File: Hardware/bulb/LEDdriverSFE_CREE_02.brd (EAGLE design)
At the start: 49 x 49 mm, 26 parts, among them U1 ZXLD1360, U2 ZXLD1360, U3 ZXLD1360, U4 ZXLD1360

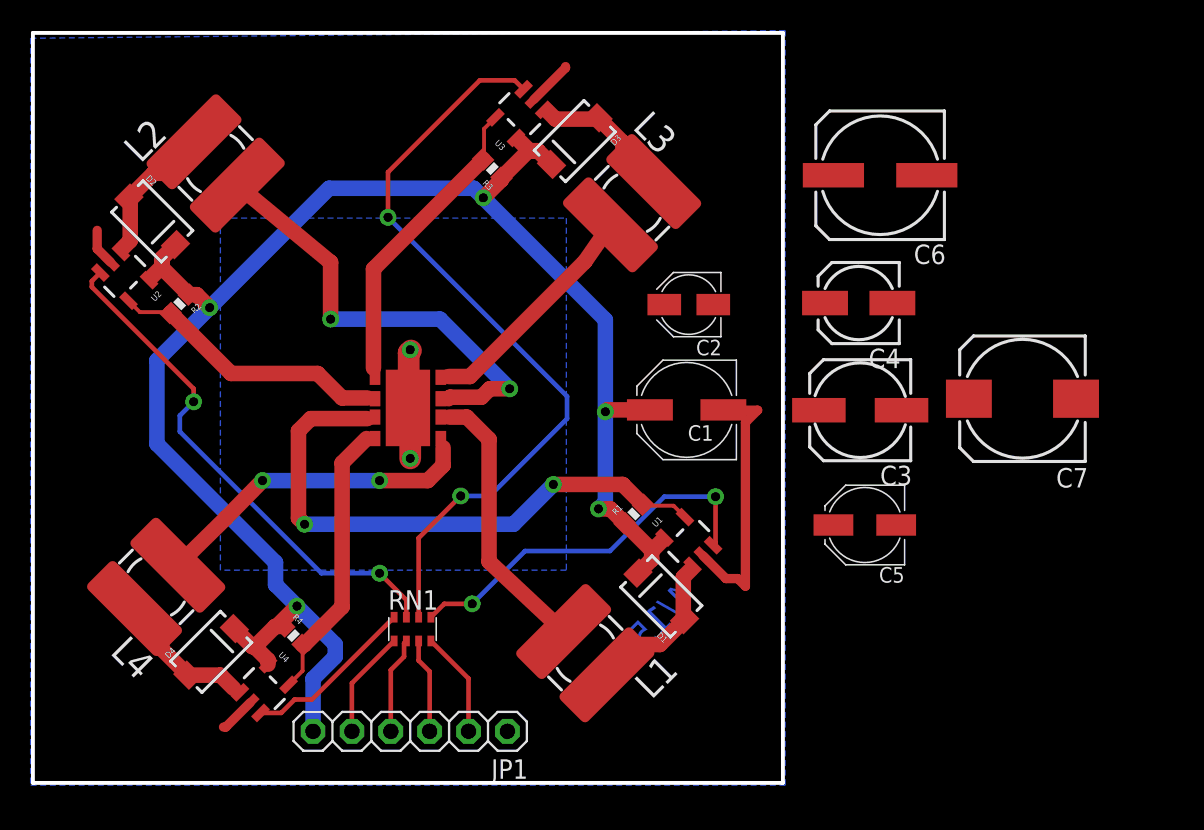
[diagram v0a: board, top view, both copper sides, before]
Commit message: added firmware version 08 and included updates to server
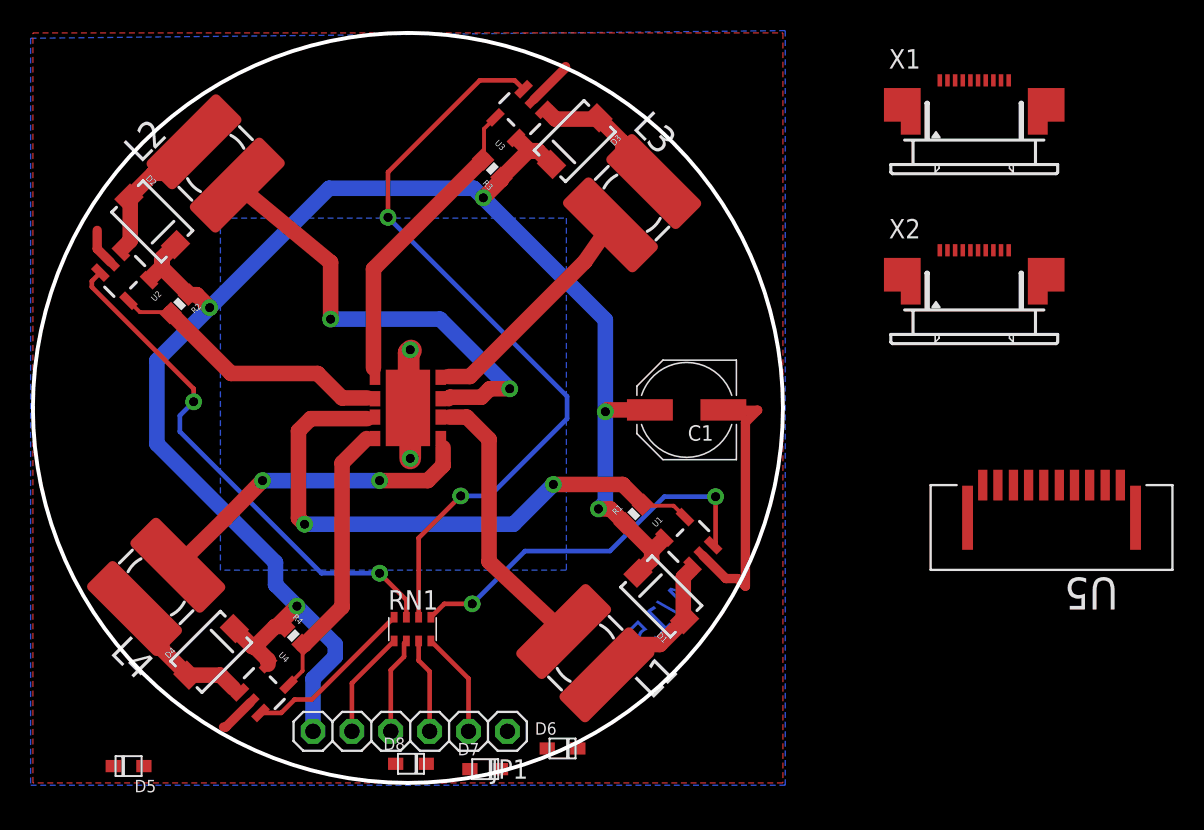
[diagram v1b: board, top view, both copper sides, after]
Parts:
- removed C2: (no value), rcl:PANASONIC_B
- removed C3: (no value), rcl:153CLV-0605
- removed C4: (no value), rcl:153CLV-0505
- removed C5: (no value), rcl:PANASONIC_C
- removed C6: (no value), rcl:153CLV-0807
- removed C7: (no value), rcl:175TMP-0808
- added D5, D6, D7, D8: (no value), adafruit:SOD-323F
- added U5: SFW10R-1STE1LF, FCI_By_element14_Batch_1:FCI_SFW10R-1STE1LF
- added X1, X2: 52745-1090, con-molex:52745-1090
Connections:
- removed net N$15: JP1.5, RN1.1
- removed net N$18: JP1.3, RN1.3
- new net BLUEIN: D7.C, JP1.4, RN1.2
- new net D+IN: X1.7, X2.7
- new net D-IN: X1.8, X2.8
- new net D10: X1.4, X2.4
- new net D13: X1.2, X2.2
- new net D5: X1.3, X2.3
- new net D9: X1.5, X2.5
- new net GREENIN: D6.C, JP1.2, RN1.4
- new net N$20: D7.A
- new net N$21: D8.A
- new net RAW: X1.10, X2.10
- new net REDIN: D5.C, JP1.5, RN1.1
- new net TXLED: X1.6, X2.6
- new net UVCC: X1.1, X2.1
- new net WHITEIN: D8.C, JP1.3, RN1.3
- net GND: now also X1.9, X2.9
- net N$14: now also D5.A; no longer JP1.2, RN1.4
- net N$17: now also D6.A; no longer JP1.4, RN1.2
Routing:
- net REDIN: track 0.00 -> 7.05 mm
- net N$15: track 7.05 -> 0.00 mm
- net N$14: track 6.92 -> 0.00 mm
- net GREENIN: track 0.00 -> 6.92 mm
- net N$17: track 6.33 -> 0.00 mm
- net BLUEIN: track 0.00 -> 6.33 mm
- net WHITEIN: track 0.00 -> 6.20 mm
- net N$18: track 6.20 -> 0.00 mm
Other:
- outline, holes or cut-outs redrawn
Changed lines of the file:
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@@
 <?xml version="1.0" encoding="utf-8"?>
 <!DOCTYPE eagle SYSTEM "eagle.dtd">
-<eagle version="6.2">
+<eagle version="6.4">
 <drawing>
 <settings>
@@
 <layer number="19" name="Unrouted" color="12" fill="1" visible="yes" active="yes"/>
 <layer number="20" name="Dimension" color="15" fill="1" visible="yes" active="yes"/>
-<layer number="21" name="tPlace" color="16" fill="1" visible="yes" active="yes"/>
+<layer number="21" name="tPlace" color="16" fill="1" visible="no" active="yes"/>
 <layer number="22" name="bPlace" color="14" fill="1" visible="no" active="yes"/>
 <layer number="23" name="tOrigins" color="15" fill="1" visible="yes" active="yes"/>
@@
 <text x="-4.191" y="19.431" size="1.778" layer="22" ratio="15" rot="SMR270">GND</text>
 <text x="8.001" y="21.971" size="1.27" layer="22" ratio="15" rot="SMR270">12-30V</text>
-<wire x1="0" y1="49" x2="49" y2="49" width="0.254" layer="20"/>
-<wire x1="49" y1="49" x2="49" y2="0" width="0.254" layer="20"/>
-<wire x1="49" y1="0" x2="0" y2="0" width="0.254" layer="20"/>
-<wire x1="0" y1="0" x2="0" y2="49" width="0.254" layer="20"/>
 <rectangle x1="3" y1="30.85" x2="8.4" y2="35.55" layer="41"/>
 <rectangle x1="12.85" y1="4" x2="17.4" y2="8.45" layer="41"/>
@@
 <rectangle x1="28.9" y1="41.4" x2="34.5" y2="46.4" layer="41"/>
 <rectangle x1="20.75" y1="21.4" x2="27.75" y2="28.2" layer="41"/>
+<wire x1="0" y1="24.5" x2="24.5" y2="49" width="0.254" layer="20" curve="-90"/>
+<wire x1="0" y1="24.5" x2="24.5" y2="0" width="0.254" layer="20" curve="90"/>
+<wire x1="49" y1="24.5" x2="24.5" y2="0" width="0.254" layer="20" curve="-90"/>
+<wire x1="49" y1="24.5" x2="24.5" y2="49" width="0.254" layer="20" curve="90"/>
 </plain>
 <attributes>
@@
 <class number="0" name="default" width="0" drill="0">
 </class>
+<class number="1" name="vcc" width="0" drill="0">
+</class>
 </classes>
-<designrules>
+<designrules name="default">
 <description language="en">&lt;b&gt;EAGLE Design Rules&lt;/b&gt;
 &lt;p&gt;
@@
 <attribute name="OC_FARNELL" value="unknown" x="24.8" y="10.05" size="1.778" layer="27" display="off"/>
 </element>
-<element name="C2" library="rcl" package="PANASONIC_B" value="" x="42.85" y="31.25" rot="R180"/>
-<element name="C3" library="rcl" package="153CLV-0605" value="" x="54.05" y="24.35" rot="R180"/>
-<element name="C4" library="rcl" package="153CLV-0505" value="" x="53.95" y="31.35" rot="R180"/>
-<element name="C5" library="rcl" package="PANASONIC_C" value="" x="54.35" y="16.85" rot="R180"/>
-<element name="C6" library="rcl" package="153CLV-0807" value="" x="55.35" y="39.7" rot="R180"/>
-<element name="C7" library="rcl" package="175TMP-0808" value="" x="64.65" y="25.1" rot="R180"/>
+<element name="D5" library="adafruit" package="SOD-323F" value="" x="6.25" y="1.1" rot="R180"/>
+<element name="D6" library="adafruit" package="SOD-323F" value="" x="34.6" y="2.25"/>
+<element name="D7" library="adafruit" package="SOD-323F" value="" x="29.55" y="0.9"/>
+<element name="D8" library="adafruit" package="SOD-323F" value="" x="24.7" y="1.25"/>
+<element name="X1" library="con-molex" package="52745-1090" value="52745-1090" x="61.5" y="43.4">
+<attribute name="OC_NEWARK" value="92M6380" x="61.5" y="43.4" size="1.778" layer="27" display="off"/>
+<attribute name="MPN" value="52745-1090" x="61.5" y="43.4" size="1.778" layer="27" display="off"/>
+<attribute name="MF" value="" x="61.5" y="43.4" size="1.778" layer="27" display="off"/>
+<attribute name="OC_FARNELL" value="unknown" x="61.5" y="43.4" size="1.778" layer="27" display="off"/>
+</element>
+<element name="X2" library="con-molex" package="52745-1090" value="52745-1090" x="61.5" y="32.3">
+<attribute name="OC_NEWARK" value="92M6380" x="61.5" y="32.3" size="1.778" layer="27" display="off"/>
+<attribute name="MPN" value="52745-1090" x="61.5" y="32.3" size="1.778" layer="27" display="off"/>
+<attribute name="MF" value="" x="61.5" y="32.3" size="1.778" layer="27" display="off"/>
+<attribute name="OC_FARNELL" value="unknown" x="61.5" y="32.3" size="1.778" layer="27" display="off"/>
+</element>
+<element name="U5" library="FCI_By_element14_Batch_1" package="FCI_SFW10R-1STE1LF" value="SFW10R-1STE1LF" x="66.55" y="22.2" rot="R180">
+<attribute name="PACKAGE" value="CONNECTOR - 10POS" x="66.55" y="22.2" size="1.778" layer="27" rot="R180" display="off"/>
+<attribute name="OC_NEWARK" value="62K5594" x="66.55" y="22.2" size="1.778" layer="27" rot="R180" display="off"/>
+<attribute name="MPN" value="SFW10R-1STE1LF" x="66.55" y="22.2" size="1.778" layer="27" rot="R180" display="off"/>
+<attribute name="SUPPLIER" value="FCI" x="66.55" y="22.2" size="1.778" layer="27" rot="R180" display="off"/>
+<attribute name="OC_FARNELL" value="1632207" x="66.55" y="22.2" size="1.778" layer="27" rot="R180" display="off"/>
+</element>
 </elements>
 <signals>
@@
 <wire x1="46.55" y1="12.85" x2="46.05" y2="13.35" width="0.6096" layer="1"/>
 <wire x1="46.05" y1="13.35" x2="45.274978125" y2="13.35" width="0.6096" layer="1"/>
+<contactref element="X1" pad="9"/>
+<contactref element="X2" pad="9"/>
+<wire x1="45.11" y1="24.37" x2="32.72790625" y2="44.647090625" width="0" layer="19" extent="1-1"/>
+<wire x1="31" y1="3.37" x2="43.768559375" y2="14.85641875" width="0" layer="19" extent="1-1"/>
+<wire x1="14.1968" y1="5.245009375" x2="31" y2="3.37" width="0" layer="19" extent="1-1"/>
+<wire x1="5.078571875" y1="34.013359375" x2="32.72790625" y2="44.647090625" width="0" layer="19" extent="1-1"/>
+<wire x1="63.25" y1="45.9" x2="12.45" y2="3.65" width="0" layer="19" extent="1-1"/>
+<wire x1="63.25" y1="34.8" x2="63.25" y2="45.9" width="0" layer="19" extent="1-1"/>
 </signal>
 <signal name="VIN">
@@
 <wire x1="16.223259375" y1="4.573259375" x2="14.868553125" y2="4.573259375" width="0.3048" layer="1"/>
 </signal>
-<signal name="N$14">
+<signal name="GREENIN">
 <contactref element="RN1" pad="4"/>
 <contactref element="JP1" pad="2"/>
 <wire x1="28.46" y1="3.37" x2="28.46" y2="6.815" width="0.3048" layer="1"/>
 <wire x1="28.46" y1="6.815" x2="26" y2="9.275" width="0.3048" layer="1"/>
-</signal>
-<signal name="N$15">
+<contactref element="D6" pad="C"/>
+<wire x1="28.46" y1="3.37" x2="35.6" y2="2.25" width="0" layer="19" extent="1-1"/>
+</signal>
+<signal name="REDIN">
 <contactref element="RN1" pad="1"/>
 <contactref element="JP1" pad="5"/>
 <wire x1="20.84" y1="3.37" x2="20.84" y2="6.515" width="0.3048" layer="1"/>
 <wire x1="20.84" y1="6.515" x2="23.6" y2="9.275" width="0.3048" layer="1"/>
-</signal>
-<signal name="N$17">
+<contactref element="D5" pad="C"/>
+<wire x1="5.25" y1="1.1" x2="20.84" y2="3.37" width="0" layer="19" extent="1-1"/>
+</signal>
+<signal name="BLUEIN">
 <contactref element="RN1" pad="2"/>
 <contactref element="JP1" pad="4"/>
@@
 <wire x1="24.25" y1="8.25" x2="24.25" y2="9.125" width="0.3048" layer="1"/>
 <wire x1="24.25" y1="9.125" x2="24.4" y2="9.275" width="0.3048" layer="1"/>
-</signal>
-<signal name="N$18">
+<contactref element="D7" pad="C"/>
+<wire x1="23.38" y1="3.37" x2="30.55" y2="0.9" width="0" layer="19" extent="1-1"/>
+</signal>
+<signal name="WHITEIN">
 <contactref element="RN1" pad="3"/>
 <contactref element="JP1" pad="3"/>
@@
 <wire x1="25.92" y1="7.28" x2="25.2" y2="8" width="0.3048" layer="1"/>
 <wire x1="25.2" y1="8" x2="25.2" y2="9.275" width="0.3048" layer="1"/>
+<contactref element="D8" pad="C"/>
+<wire x1="25.92" y1="3.37" x2="25.7" y2="1.25" width="0" layer="19" extent="1-1"/>
 </signal>
 <signal name="N$1">
@@
 <signal name="N$10">
 </signal>
+<signal name="N$14">
+<contactref element="D5" pad="A"/>
+</signal>
+<signal name="N$17">
+<contactref element="D6" pad="A"/>
+</signal>
+<signal name="N$20">
+<contactref element="D7" pad="A"/>
+</signal>
+<signal name="N$21">
+<contactref element="D8" pad="A"/>
+</signal>
+<signal name="D9">
+<contactref element="X1" pad="5"/>
+<contactref element="X2" pad="5"/>
+<wire x1="61.25" y1="45.9" x2="61.25" y2="34.8" width="0" layer="19" extent="1-1"/>
+</signal>
+<signal name="D5">
+<contactref element="X1" pad="3"/>
+<contactref element="X2" pad="3"/>
+<wire x1="60.25" y1="45.9" x2="60.25" y2="34.8" width="0" layer="19" extent="1-1"/>
+</signal>
+<signal name="D10">
+<contactref element="X1" pad="4"/>
+<contactref element="X2" pad="4"/>
+<wire x1="60.75" y1="45.9" x2="60.75" y2="34.8" width="0" layer="19" extent="1-1"/>
+</signal>
+<signal name="UVCC">
+<contactref element="X1" pad="1"/>
+<contactref element="X2" pad="1"/>
+<wire x1="59.25" y1="45.9" x2="59.25" y2="34.8" width="0" layer="19" extent="1-1"/>
+</signal>
+<signal name="D13">
+<contactref element="X1" pad="2"/>
+<contactref element="X2" pad="2"/>
+<wire x1="59.75" y1="45.9" x2="59.75" y2="34.8" width="0" layer="19" extent="1-1"/>
+</signal>
+<signal name="TXLED">
+<contactref element="X1" pad="6"/>
+<contactref element="X2" pad="6"/>
+<wire x1="61.75" y1="45.9" x2="61.75" y2="34.8" width="0" layer="19" extent="1-1"/>
+</signal>
+<signal name="RAW">
+<contactref element="X1" pad="10"/>
+<contactref element="X2" pad="10"/>
+<wire x1="63.75" y1="45.9" x2="63.75" y2="34.8" width="0" layer="19" extent="1-1"/>
+</signal>
+<signal name="D+IN">
+<contactref element="X1" pad="7"/>
+<contactref element="X2" pad="7"/>
+<wire x1="62.25" y1="45.9" x2="62.25" y2="34.8" width="0" layer="19" extent="1-1"/>
+</signal>
+<signal name="D-IN">
+<contactref element="X1" pad="8"/>
+<contactref element="X2" pad="8"/>
+<wire x1="62.75" y1="45.9" x2="62.75" y2="34.8" width="0" layer="19" extent="1-1"/>
+</signal>
 </signals>

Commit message: updates to api docs and file
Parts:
- removed JP1: (no value), adafruit:1X06
- removed U5: SFW10R-1STE1LF, FCI_By_element14_Batch_1:FCI_SFW10R-1STE1LF
- removed X2: 52745-1090, con-molex:52745-1090
- moved X1 54.4 mm to (24.5, 3.50)
- moved D5 18.7 mm to (22.4, 10.3), turned to 270 degrees
- moved D6 12.9 mm to (22.9, 7.80)
- moved D7 9.78 mm to (27.1, 10.3), turned to 270 degrees
- moved D8 6.85 mm to (26.7, 7.80), turned to 180 degrees
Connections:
- net ADJ3 renamed WHITE
- removed net ADJ1: RN1.5, U1.3
- removed net ADJ2: RN1.7, U2.3
- removed net BLUEIN: D7.C, JP1.4, RN1.2
- removed net GREENIN: D6.C, JP1.2, RN1.4
- removed net N$13: RN1.8, U4.3
- removed net N$14: D5.A
- removed net N$17: D6.A
- removed net N$20: D7.A
- removed net N$21: D8.A
- removed net RAW: X1.10, X2.10
- removed net REDIN: D5.C, JP1.5, RN1.1
- removed net WHITEIN: D8.C, JP1.3, RN1.3
- new net BLUE: RN1.8, U2.3
- new net GREEN: RN1.7, U1.3
- new net RED: RN1.5, U4.3
- net D+IN: now also X1.4; no longer X1.7, X2.7
- net D-IN: now also X1.3; no longer X1.8, X2.8
- net D10: now also D6.C, RN1.2, X1.7; no longer X1.4, X2.4
- net D13: now also D7.C, RN1.4, X1.9; no longer X1.2, X2.2
- net D5: now also D8.C, RN1.3, X1.8; no longer X1.3, X2.3
- net D9: now also D5.C, RN1.1, X1.6; no longer X1.5, X2.5
- net GND: now also D5.A, D6.A, D7.A, D8.A, X1.2; no longer JP1.1, X1.9, X2.9
- net TXLED: now also X1.5; no longer X1.6, X2.6
- net UVCC: now also X1.10; no longer X1.1, X2.1
- net VIN: now also X1.1; no longer JP1.6
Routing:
- net BLUE: track 0.00 -> 34.9 mm, vias 0 -> 2
- net ADJ2: track 34.2 -> 0.00 mm, vias 2 -> 0
- net GREEN: track 0.00 -> 27.3 mm, vias 0 -> 2
- net ADJ1: track 25.1 -> 0.00 mm, vias 2 -> 0
- net GND: track 25.6 -> 8.13 mm, vias 0 -> 2
- net RED: track 0.00 -> 14.3 mm
- net N$13: track 11.3 -> 0.00 mm
- net REDIN: track 7.05 -> 0.00 mm
- net GREENIN: track 6.92 -> 0.00 mm
- net BLUEIN: track 6.33 -> 0.00 mm
- net D9: track 0.00 -> 6.23 mm
- net WHITEIN: track 6.20 -> 0.00 mm
- net D13: track 0.00 -> 4.50 mm
- net D10: track 0.00 -> 4.12 mm
- net D5: track 0.00 -> 3.50 mm
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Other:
- outline, holes or cut-outs redrawn
